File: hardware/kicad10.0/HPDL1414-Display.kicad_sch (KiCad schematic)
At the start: 10 parts, among them J1 Qwiic/Stemma QT, J2 Qwiic/Stemma QT, J3 SWDIO 3 Pin, U1 CH32V003AxMx

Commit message: kicad 10.0, drc passing
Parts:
- U1: footprint Package_SO:SOP-16_3.9x9.9mm_P1.27mm -> Package_SO:STC_SOP-16_3.9x9.9mm_P1.27mm; symbol MCU_WCH_CH32V0:CH32V003AxMx -> MCU_WCH_RiscV:CH32V003AxMx

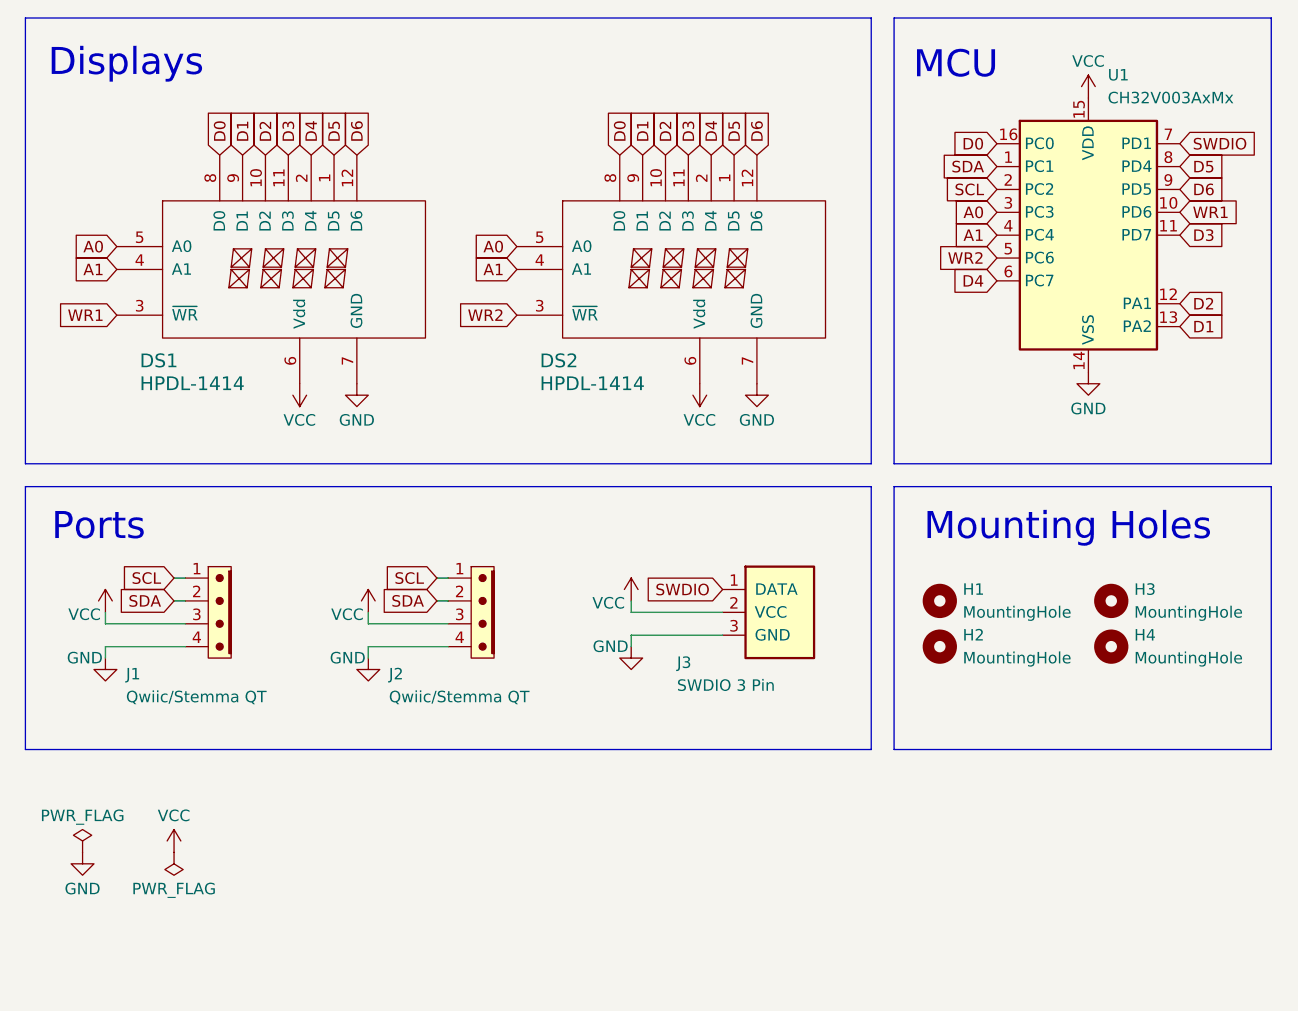
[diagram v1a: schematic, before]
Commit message: cap and debug pads
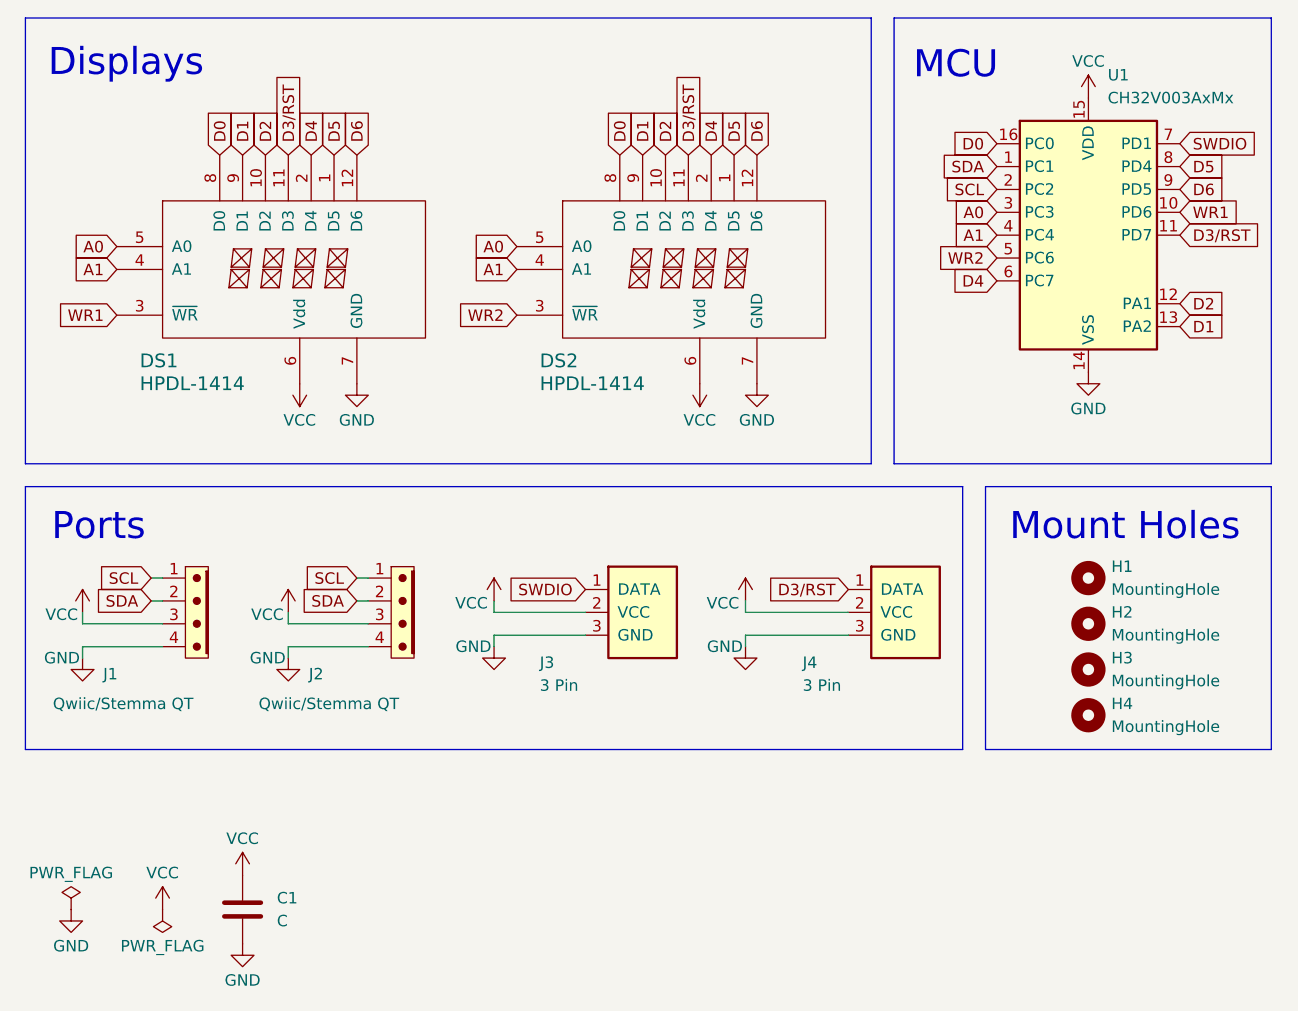
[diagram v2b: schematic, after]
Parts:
- added C1: C, Capacitor_SMD:C_0805_2012Metric, symbol Device:C
- added J4: 3 Pin, HPDL-1414:Pads_1x3_2.54mm, symbol HPDL-1414:SWDIO_3_PIN
- J3: value SWDIO 3 Pin -> 3 Pin
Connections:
- net GND: now also C1.2, J4.3 (GND)
- net VCC: now also C1.1, J4.2 (VCC)
- net D3 renamed D3/RST
- net D3/RST: now also J4.1 (DATA)
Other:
- note added: "Mount Holes"
- note removed: "Mounting Holes"
- moved on the sheet: H1, H2, H3, H4, J1, J2, J3

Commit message: adjustments
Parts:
- J3: symbol HPDL-1414:SWDIO_3_PIN -> HPDL-1414:SWDIO_3_PIN_ALT
- J4: footprint HPDL-1414:Pads_1x3_2.54mm -> NONIK0:Pads_1x3_2.54mm
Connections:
- net GND: now also J3.2 (GND); no longer J3.3 (GND)
- net SWDIO: now also J3.3 (DATA); no longer J3.1 (DATA)
- net VCC: now also J3.1 (VCC); no longer J3.2 (VCC)
